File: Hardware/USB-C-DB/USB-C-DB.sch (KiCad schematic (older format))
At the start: 45 parts, among them J1 USB_C_Receptacle, J2 BatTP+, J3 JST Battery con, J4 BatTP-, U1 FT260S-U, U3 ESP-WROOM-02

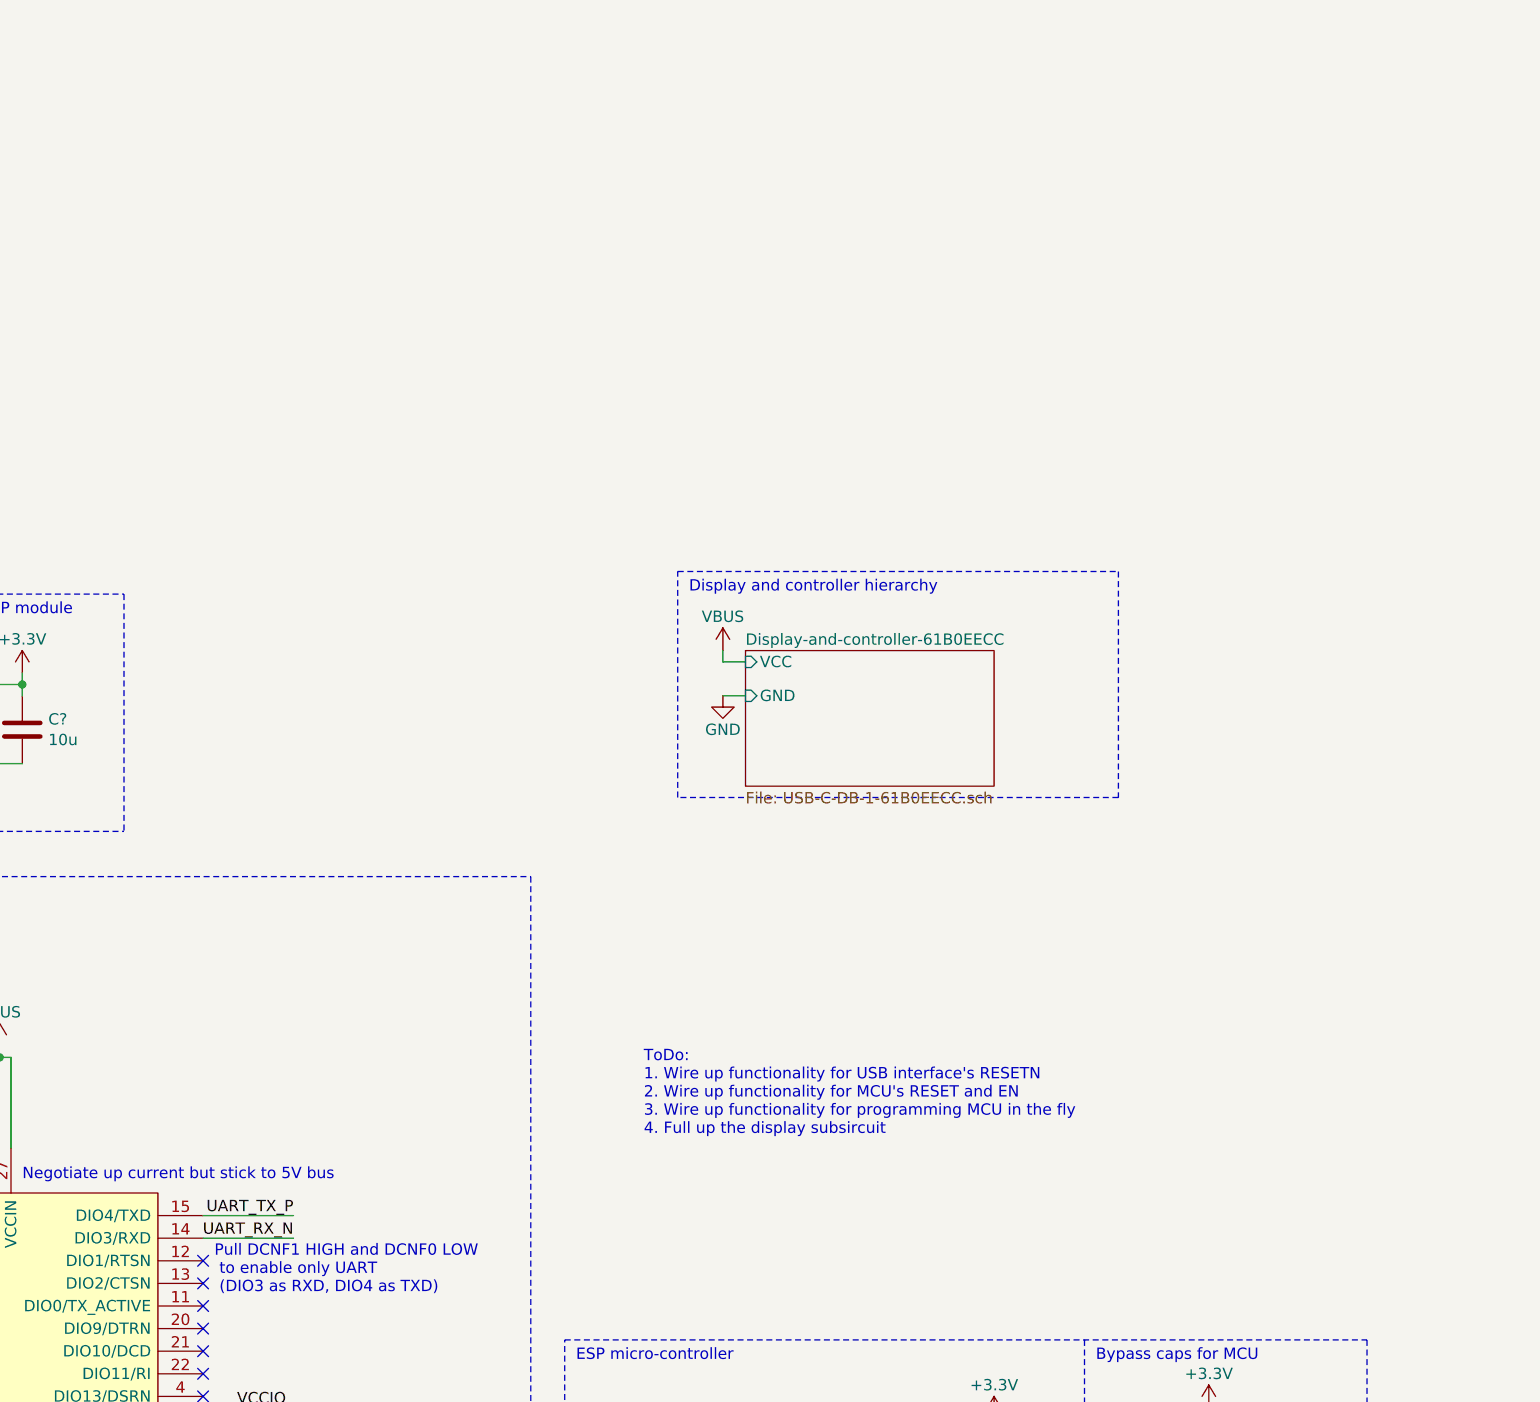
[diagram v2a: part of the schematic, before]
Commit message: Adding PWM based brightness control circuit for display
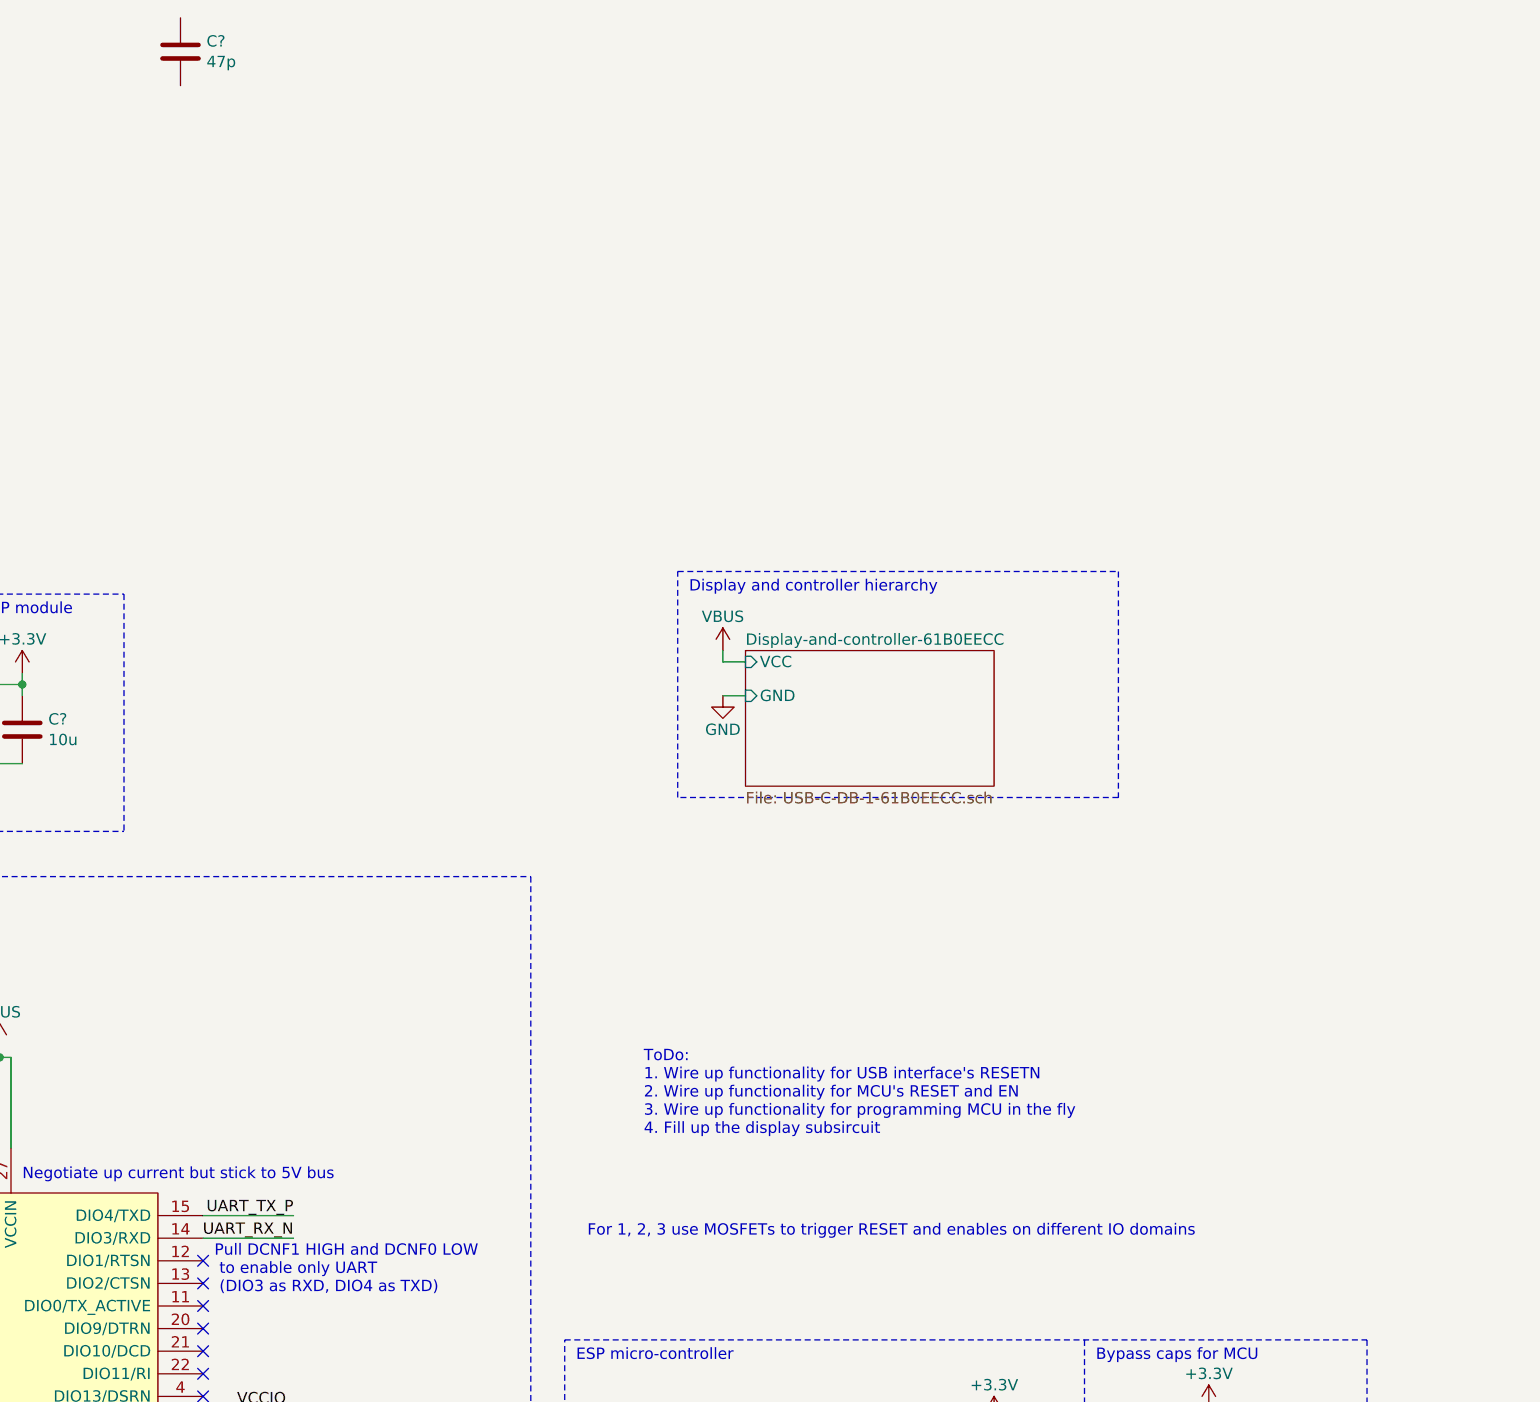
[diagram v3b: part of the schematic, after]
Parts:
- added C?: 47p, Capacitor_SMD:C_0402_1005Metric_Pad0.74x0.62mm_HandSolder, symbol Device:C
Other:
- note added: "For 1, 2, 3 use MOSFETs to trigger RESET and enables on different IO domains"
- note added: "ToDo:\n1. Wire up functionality for USB interface's RESETN\n2. Wire up functionality for MCU's RESET and EN\n3. Wire up functionality for programming MCU in the fly\n4. Fill up the display subsircuit"
- note removed: "ToDo:\n1. Wire up functionality for USB interface's RESETN\n2. Wire up functionality for MCU's RESET and EN\n3. Wire up functionality for programming MCU in the fly\n4. Full up the display subsircuit"
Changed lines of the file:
@@
 	6100 4550 6100 4500
 Text Notes 7900 3300 0    50   ~ 0
-ToDo:\n1. Wire up functionality for USB interface's RESETN\n2. Wire up functionality for MCU's RESET and EN\n3. Wire up functionality for programming MCU in the fly\n4. Full up the display subsircuit
+ToDo:\n1. Wire up functionality for USB interface's RESETN\n2. Wire up functionality for MCU's RESET and EN\n3. Wire up functionality for programming MCU in the fly\n4. Fill up the display subsircuit
 Text Label 3850 4050 0    50   ~ 0
 DEBUGGER
@@
 Wire Wire Line
 	3000 6550 3000 6750
+Text Notes 7650 3750 0    50   ~ 0
+For 1, 2, 3 use MOSFETs to trigger RESET and enables on different IO domains
+$Comp
+L Device:C C?
+U 1 1 62161AC5
+P 5850 -1500
+F 0 "C?" H 5965 -1454 50  0000 L CNN
+F 1 "47p" H 5965 -1545 50  0000 L CNN
+F 2 "Capacitor_SMD:C_0402_1005Metric_Pad0.74x0.62mm_HandSolder" H 5888 -1650 50  0001 C CNN
+F 3 "https://www.mouser.in/datasheet/2/212/KEM_C1003_C0G_SMD-1101588.pdf" H 5850 -1500 50  0001 C CNN
+F 4 "C0402C470J5GAC" H 5850 -1500 50  0001 C CNN "MPN"
+	1    5850 -1500
+	1    0    0    -1
+$EndComp
 $EndSCHEMATC

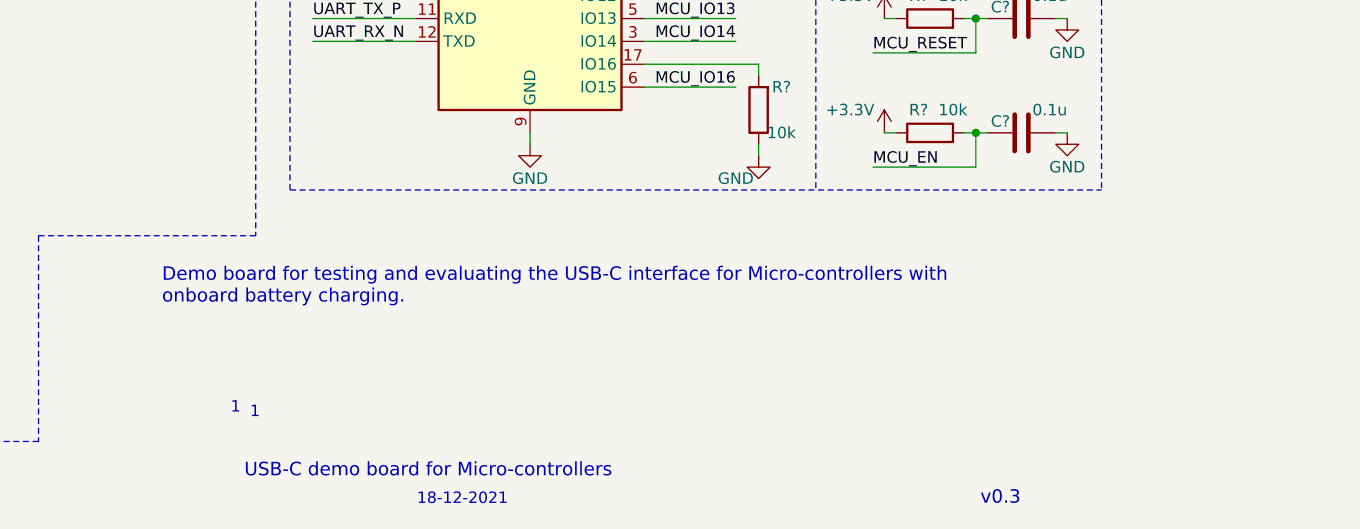
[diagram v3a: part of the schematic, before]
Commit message: Adding LED array to display subsection
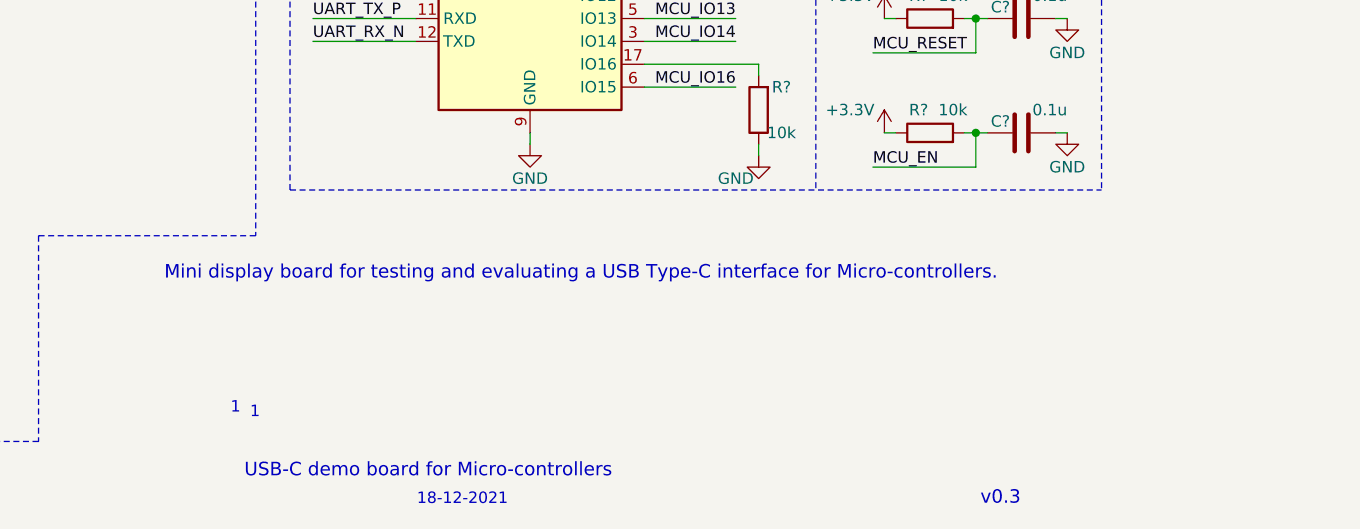
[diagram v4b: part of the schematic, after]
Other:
- note added: "Mini display board for testing and evaluating a USB Type-C interface for Micro-controllers."
- note removed: "Demo board for testing and evaluating the USB-C interface for Micro-controllers with \nonboard battery charging."
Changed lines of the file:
@@
 Text Notes 7375 7255 0    50   ~ 0
 1
-Text Notes 6990 6755 0    59   ~ 0
-Demo board for testing and evaluating the USB-C interface for Micro-controllers with \nonboard battery charging.
+Text Notes 7000 6650 0    59   ~ 0
+Mini display board for testing and evaluating a USB Type-C interface for Micro-controllers.
 $Comp
 L USB-C-DB-rescue:USB_C_Receptacle-Connector J1

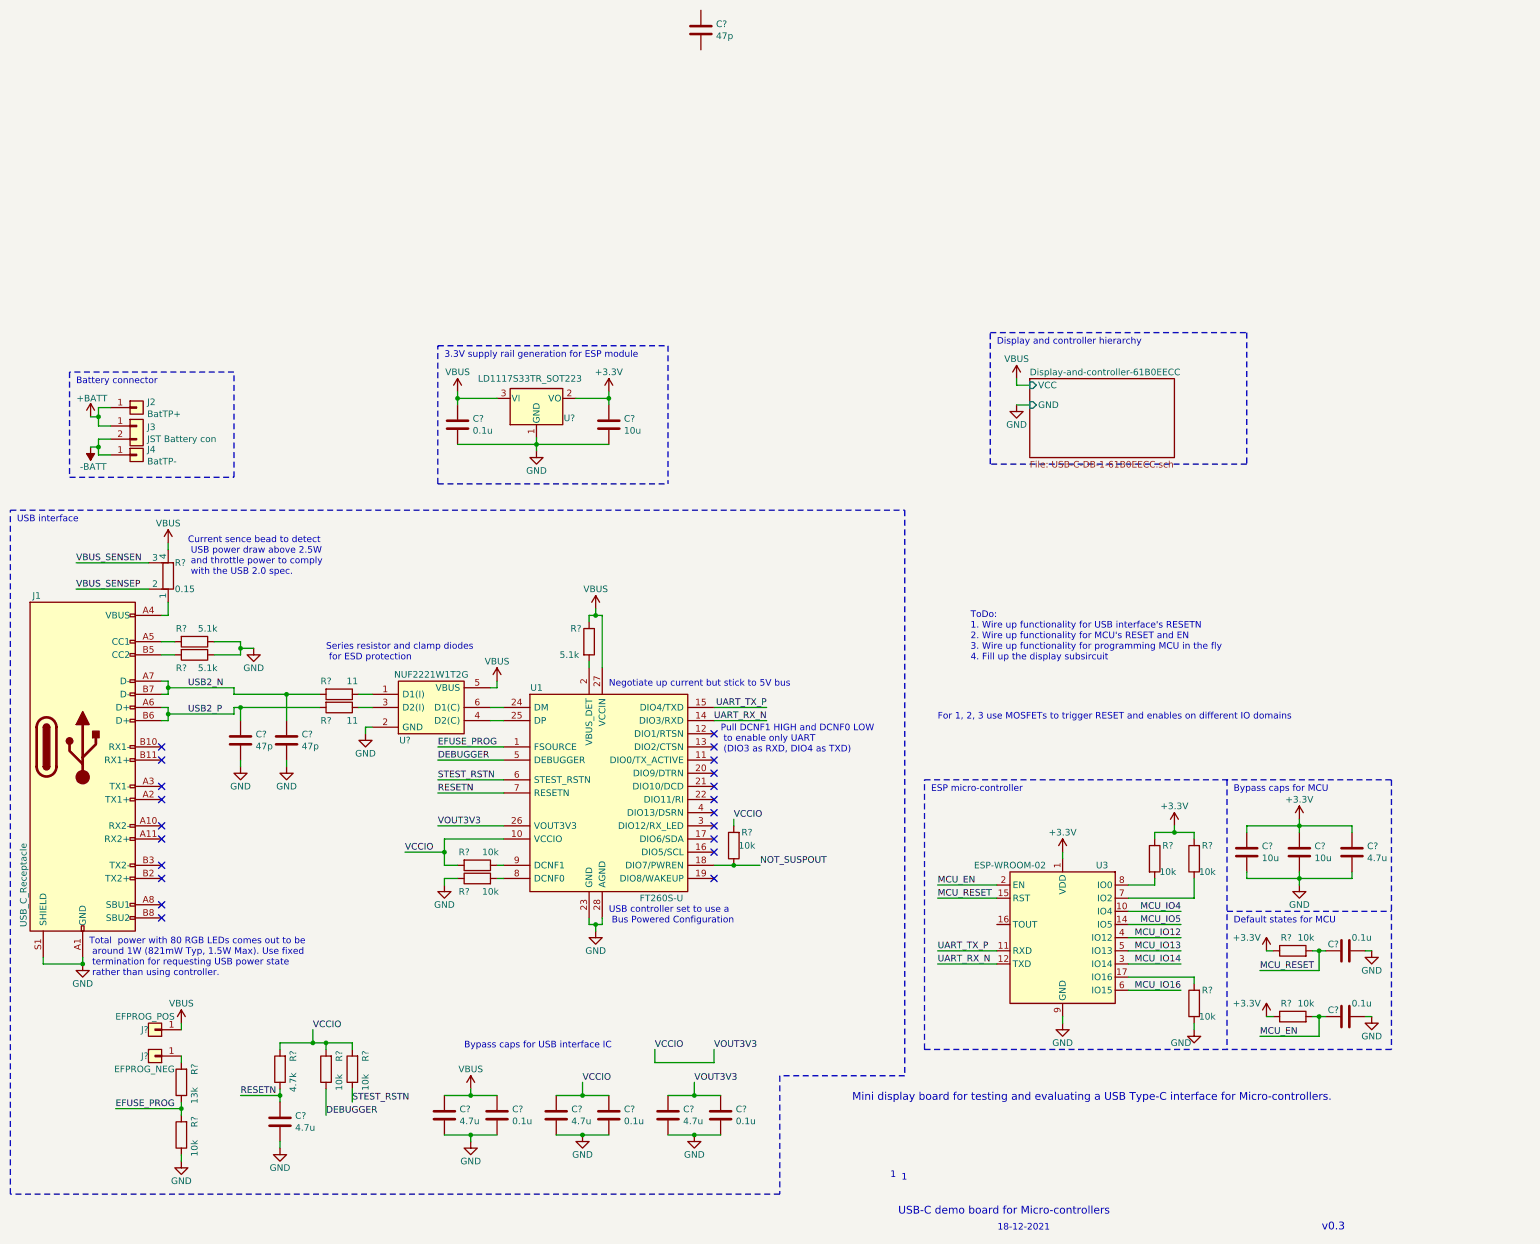
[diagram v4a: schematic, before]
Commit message: Wiring up display subsection
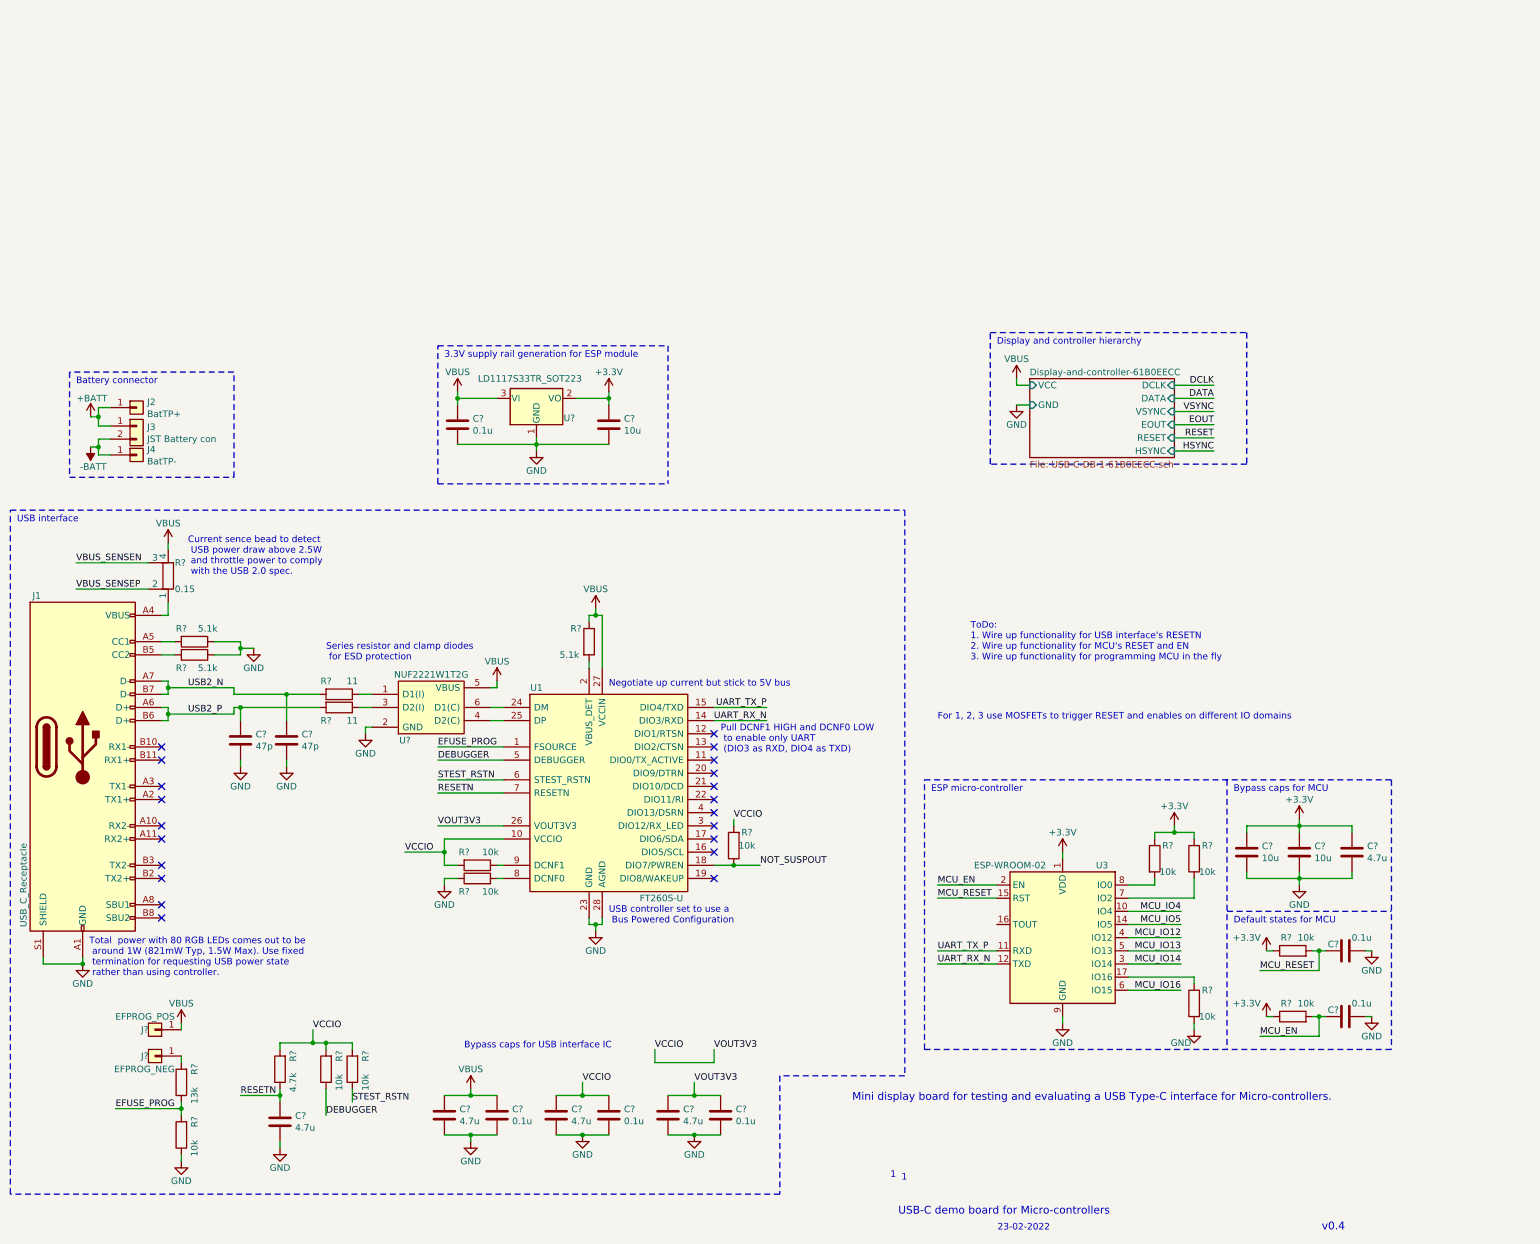
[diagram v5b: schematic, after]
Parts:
- removed C?: 47p, Capacitor_SMD:C_0402_1005Metric_Pad0.74x0.62mm_HandSolder, symbol Device:C
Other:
- note added: "23-02-2022"
- note added: "ToDo:\n1. Wire up functionality for USB interface's RESETN\n2. Wire up functionality for MCU's RESET and EN\n3. Wire up functionality for programming MCU in the fly"
- note added: "v0.4"
- note removed: "18-12-2021"
- note removed: "ToDo:\n1. Wire up functionality for USB interface's RESETN\n2. Wire up functionality for MCU's RESET and EN\n3. Wire up functionality for programming MCU in the fly\n4. Fill up the display subsircuit"
- note removed: "v0.3"
